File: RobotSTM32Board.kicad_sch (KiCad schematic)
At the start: 74 parts, among them IC1 TB6612FNG, IC2 TB6612FNG, J1 MotorA, J10 Qwiik1, J11 Qwiik2, J12 Qwiik3, J13 Qwiik4, J14 Qwiik5, J2 MotorB, J3 MotorC, J4 MotorD, J5 EncoderA, J6 EncoderB, J7 EncoderC, J8 EncoderD, J9 ESTOP, Q1 NPN, Q2 NMOS_Substrate, Q3 NMOS_Substrate, U1 NUCLEO-F411RE, U3 TPS564252DRLR, U4 TPS51386RJNR, U5 LM27403SQ/NOPB

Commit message: .
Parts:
- added J15: DCIn, Connector_JST:JST_XH_B2B-XH-AM_1x02_P2.50mm_Vertical, symbol Connector:Conn_01x02_Socket
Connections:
- net GND: now also U5.6 (SYNC)
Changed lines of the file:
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@@
 	)
 	(junction
+		(at 396.24 173.99)
+		(diameter 0)
+		(color 0 0 0 0)
+	)
+	(junction
 		(at 283.21 234.95)
 		(diameter 0)
@@
 	(wire
 		(pts
+			(xy 425.45 92.71) (xy 396.24 92.71)
+		)
+		(stroke
+			(width 0)
+			(type default)
+		)
+	)
+	(wire
+		(pts
 			(xy 25.4 21.59) (xy 25.4 25.4)
 		)
@@
 	(wire
 		(pts
-			(xy 381 173.99) (xy 407.67 173.99)
+			(xy 381 173.99) (xy 396.24 173.99)
 		)
 		(stroke
@@
 	(wire
 		(pts
+			(xy 396.24 92.71) (xy 396.24 173.99)
+		)
+		(stroke
+			(width 0)
+			(type default)
+		)
+	)
+	(wire
+		(pts
 			(xy 162.56 229.87) (xy 195.58 229.87)
 		)
@@
 	(wire
 		(pts
+			(xy 396.24 173.99) (xy 407.67 173.99)
+		)
+		(stroke
+			(width 0)
+			(type default)
+		)
+	)
+	(wire
+		(pts
 			(xy 303.53 242.57) (xy 303.53 243.84)
 		)
@@
 					(unit 1)
 				)
+			)
+		)
+	)
+	(symbol
+		(lib_id "Connector:Conn_01x02_Socket")
+		(at 224.79 57.15 0)
+		(unit 1)
+		(exclude_from_sim no)
+		(in_bom yes)
+		(on_board yes)
+		(dnp no)
+		(fields_autoplaced yes)
+		(property "Reference" "J15"
+			(at 226.06 57.1499 0)
+			(effects
+				(font
+					(size 1.27 1.27)
+				)
+				(justify left)
+			)
+		)
+		(property "Value" "DCIn"
+			(at 226.06 59.6899 0)
+			(effects
+				(font
+					(size 1.27 1.27)
+				)
+				(justify left)
+			)
+		)
+		(property "Footprint" "Connector_JST:JST_XH_B2B-XH-AM_1x02_P2.50mm_Vertical"
+			(at 224.79 57.15 0)
+			(effects
+				(font
+					(size 1.27 1.27)
+				)
+				(hide yes)
+			)
+		)
+		(property "Datasheet" "~"
+			(at 224.79 57.15 0)
+			(effects
+				(font
+					(size 1.27 1.27)
+				)
+				(hide yes)
+			)
+		)
+		(property "Description" "Generic connector, single row, 01x02, script generated"
+			(at 224.79 57.15 0)
+			(effects
+				(font
+					(size 1.27 1.27)
+				)
+				(hide yes)
+			)
+		)
+		(pin "2"
+		)
+		(pin "1"
+		)
+		(instances
+			(project "RobotSTM32Board"
+				(path "/ac0c4a11-3af6-428a-b627-4ab879a3dd88"
+					(reference "J15")
+					(unit 1)
+				)

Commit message: pcb routed
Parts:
- added C31, C32: 10nF, Capacitor_SMD:C_0603_1608Metric, symbol Device:C_Small
- added J16: UJC-H-G-SMT-2-P6-TR, USBCC:UJCHGSMT2P6TR, symbol UJC-H-G-SMT-2-P6-TR:UJC-H-G-SMT-2-P6-TR
- added R1, R20: 47k, Resistor_SMD:R_0603_1608Metric, symbol Device:R_Small
- added R2, R21: 20k, Resistor_SMD:R_0603_1608Metric, symbol Device:R_Small
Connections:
- net +5V: now also U1.CN7_24 (VIN)
- net ESTOP: now also U1.CN10_13 (PA6)
- net EncoderA1: now also U1.CN7_1 (PC10)
- net EncoderA2: now also U1.CN7_2 (PC11)
- net EncoderB1: now also U1.CN7_3 (PC12)
- net EncoderB2: now also U1.CN7_4 (PD2)
- net EncoderC1: now also U1.CN7_13 (PA13)
- net EncoderC2: now also U1.CN7_15 (PA14)
- net EncoderD1: now also U1.CN7_17 (PA15)
- net EncoderD2: now also U1.CN7_21 (PB7)
- net GND: now also U1.CN10_9 (GND_9), U1.CN7_19 (GND_19), U1.CN7_22 (GND_22), U1.CN7_8 (GND_8), C31.2, C32.2, R2.2, R21.2
- net MotorACCW: now also U1.CN10_15 (PA7); no longer U1.CN7_2 (PC11)
- net MotorACW: now also U1.CN10_16 (PB12); no longer U1.CN7_3 (PC12)
- net MotorBCCW: now also U1.CN10_14 (PA11); no longer U1.CN7_4 (PD2)
- net MotorBCW: now also U1.CN10_12 (PA12); no longer U1.CN7_13 (PA13)
- net MotorCCCW: now also U1.CN10_6 (PC5)
- net MotorCCW: now also U1.CN10_3 (PB8)
- net MotorDCCW: now also U1.CN10_4 (PC6)
- net MotorDCW: now also U1.CN10_1 (PC9)
- net MotorPWMA: now also U1.CN10_17 (PB6); no longer U1.CN7_1 (PC10)
- net MotorPWMB: now also U1.CN10_11 (PA5)
- net MotorPWMC: now also U1.CN10_5 (PB9)
- net MotorPWMD: now also U1.CN10_2 (PC8)
- net SCL: now also U1.CN10_23 (PA8)
- net SDA: now also U1.CN10_27 (PB4)
- net Vin: now also R1.1, R20.1; no longer U3.5 (EN)
- net at U5.7 (UVLO/EN): now also C32.1, R20.2, R21.1
- new net: C31.1, R1.2, R2.1, U3.5 (EN)
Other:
- moved on the sheet: C2, C3, C4, R10

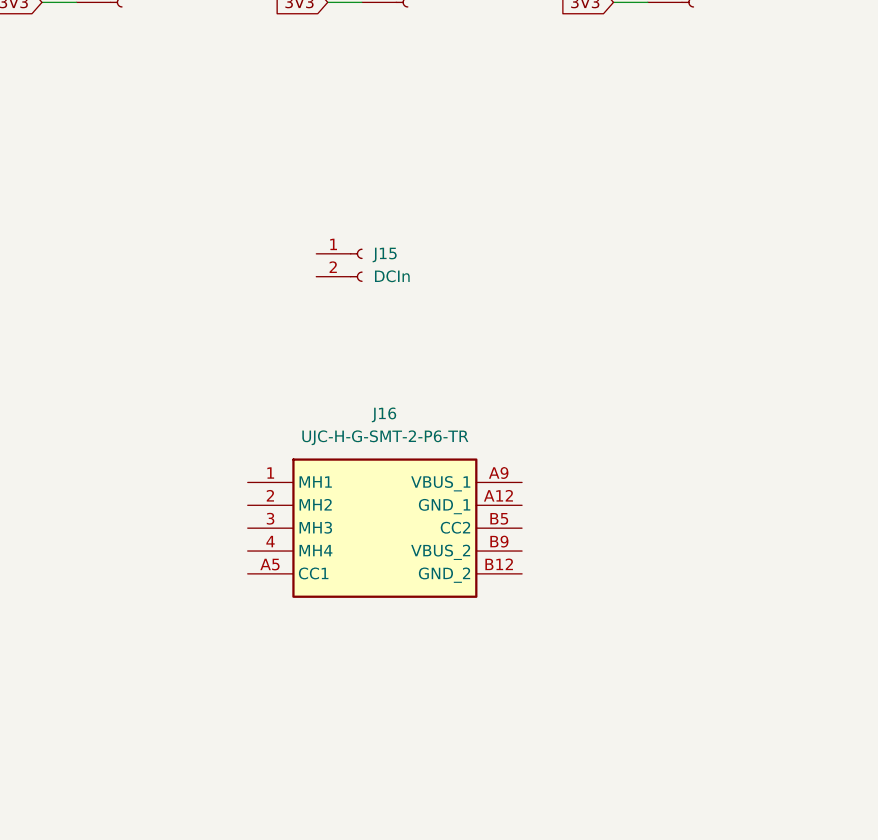
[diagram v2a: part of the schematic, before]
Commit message: correcting DRC's
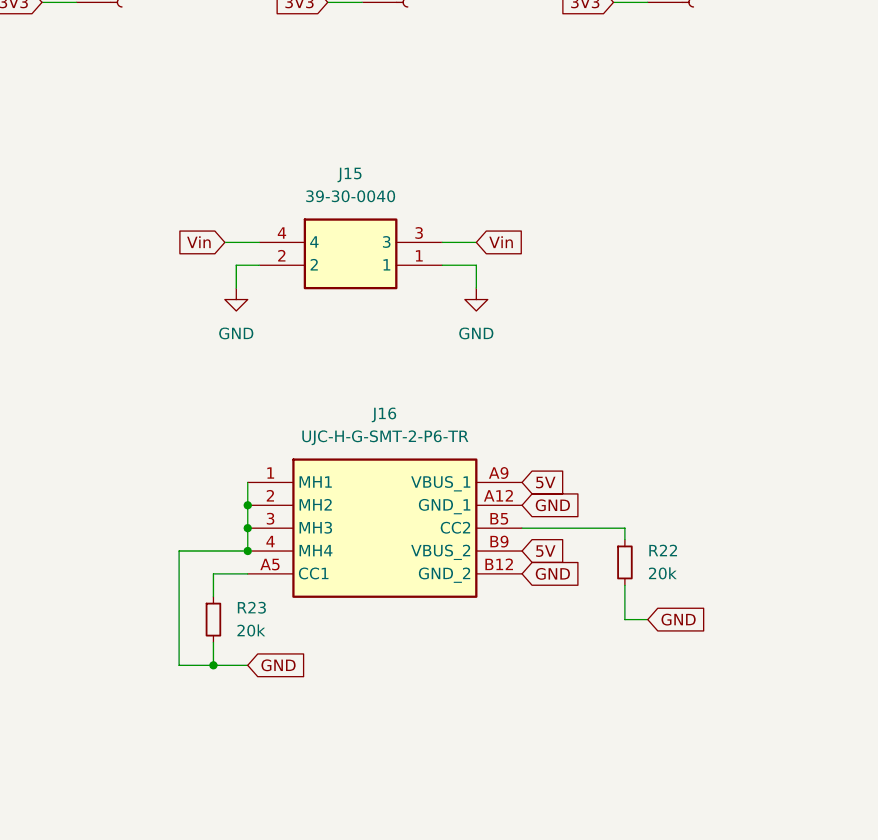
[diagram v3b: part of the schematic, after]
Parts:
- removed J15: DCIn, Connector_JST:JST_XH_B2B-XH-AM_1x02_P2.50mm_Vertical, symbol Connector:Conn_01x02_Socket
- added J15: 39-30-0040, 39-30-Y040, symbol 39-30-0040:39-30-0040
- added R22, R23: 20k, Resistor_SMD:R_0603_1608Metric, symbol Device:R_Small
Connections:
- net +5V: now also J16.A9 (VBUS_1), J16.B9 (VBUS_2)
- net GND: now also J16.1 (MH1), J16.2 (MH2), J16.3 (MH3), J16.4 (MH4), J16.A12 (GND_1), J16.B12 (GND_2), J15.1, J15.2, R22.2, R23.2
- net Vin: now also J15.3, J15.4
- net at J16.A5 (CC1): now also R23.1
- net at J16.B5 (CC2): now also R22.1

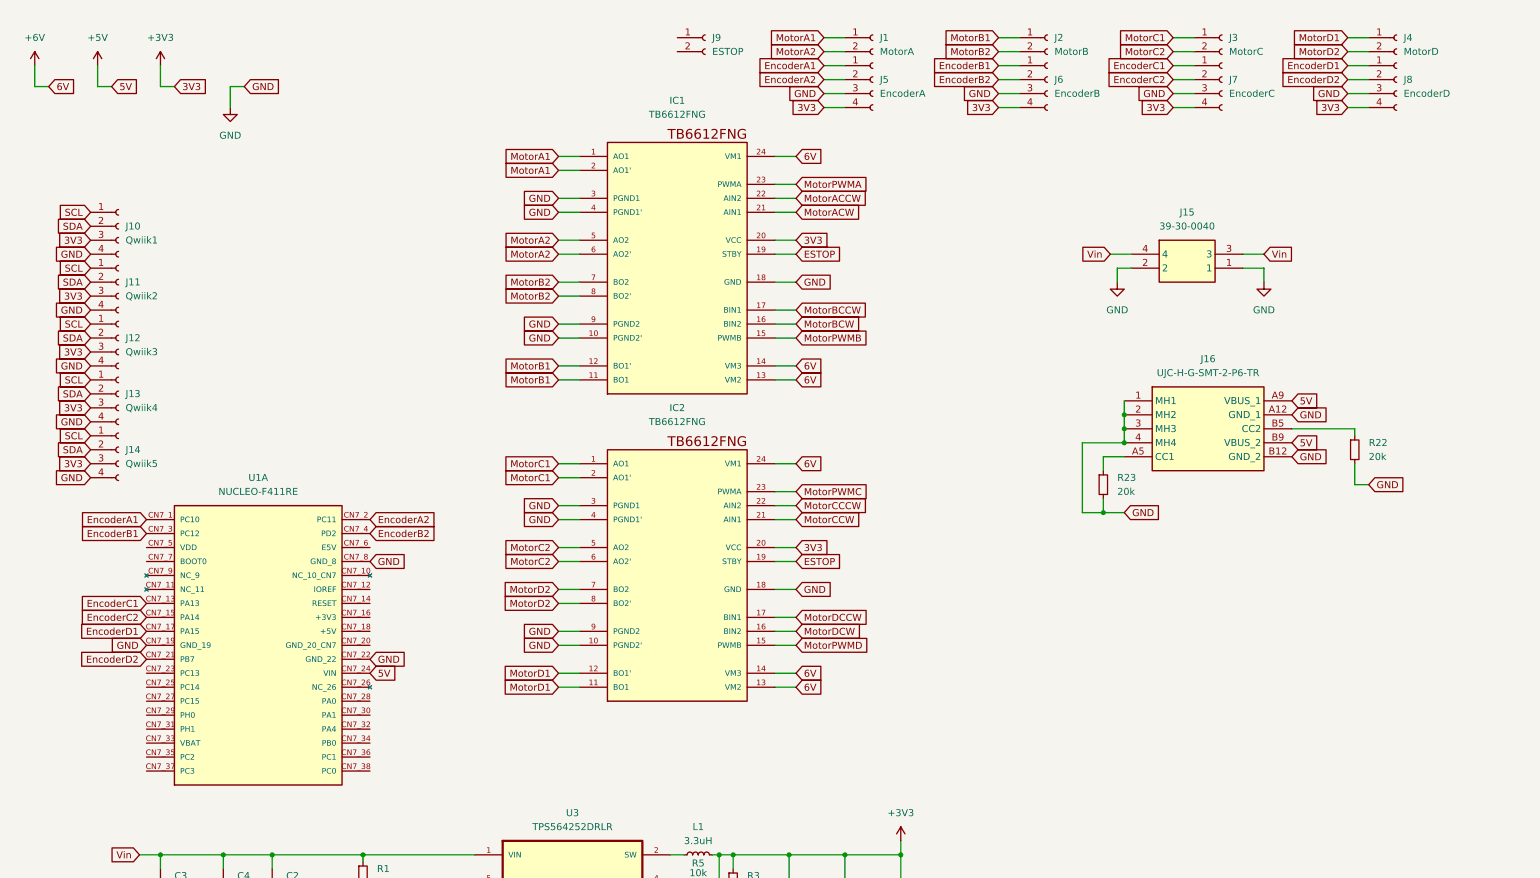
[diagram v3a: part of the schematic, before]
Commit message: Added battery connectors
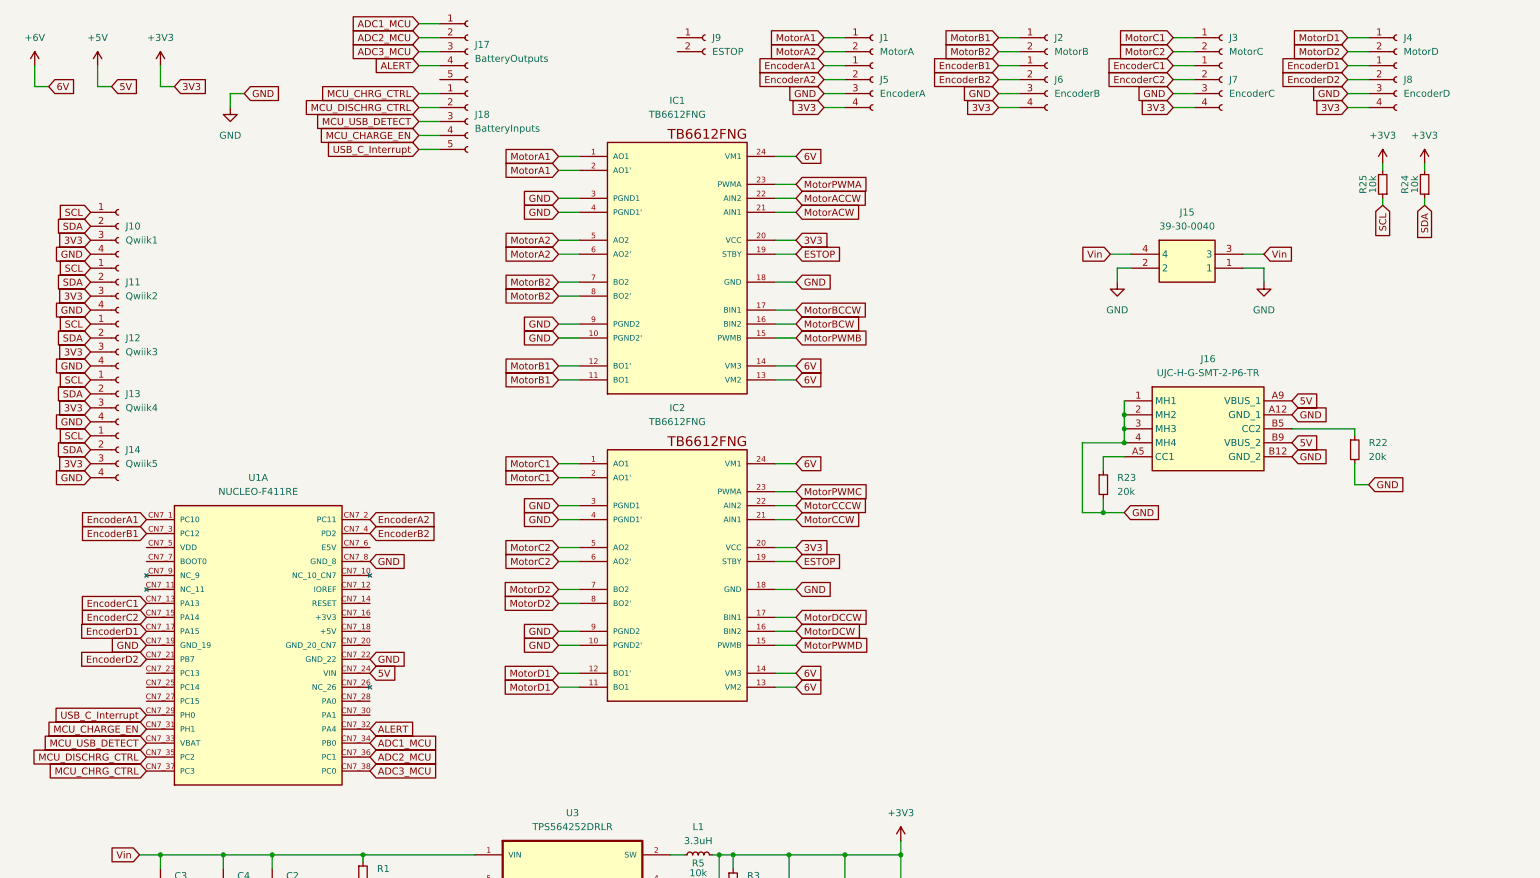
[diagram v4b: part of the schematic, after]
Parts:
- added J17: BatteryOutputs, Connector_JST:JST_SH_BM05B-SRSS-TB_1x05-1MP_P1.00mm_Vertical, symbol Connector:Conn_01x05_Socket
- added J18: BatteryInputs, Connector_JST:JST_SH_BM05B-SRSS-TB_1x05-1MP_P1.00mm_Vertical, symbol Connector:Conn_01x05_Socket
- added R24, R25: 10k, Resistor_SMD:R_0603_1608Metric, symbol Device:R_Small
- J15: footprint 39-30-Y040 -> KiCad:39-30-Y040
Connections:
- net +3V3: now also R24.2, R25.2
- net SCL: now also R25.1
- net SDA: now also R24.1
- net USB_C_Interrupt: now reaches U1.CN7_29 (PH0)
- net USB_C_Interrupt: now also J18.5 (Pin_5)
- net MCU_CHARGE_EN: now reaches U1.CN7_31 (PH1)
- net MCU_CHARGE_EN: now also J18.4 (Pin_4)
- net ALERT: now reaches U1.CN7_32 (PA4)
- net ALERT: now also J17.4 (Pin_4)
- net MCU_USB_DETECT: now reaches U1.CN7_33 (VBAT)
- net MCU_USB_DETECT: now also J18.3 (Pin_3)
- net ADC1_MCU: now reaches U1.CN7_34 (PB0)
- net ADC1_MCU: now also J17.1 (Pin_1)
- net MCU_DISCHRG_CTRL: now reaches U1.CN7_35 (PC2)
- net MCU_DISCHRG_CTRL: now also J18.2 (Pin_2)
- net ADC2_MCU: now reaches U1.CN7_36 (PC1)
- net ADC2_MCU: now also J17.2 (Pin_2)
- net MCU_CHRG_CTRL: now reaches U1.CN7_37 (PC3)
- net MCU_CHRG_CTRL: now also J18.1 (Pin_1)
- net ADC3_MCU: now reaches U1.CN7_38 (PC0)
- net ADC3_MCU: now also J17.3 (Pin_3)

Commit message: added fuse
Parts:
- added F1: 5A, symbol Device:Fuse_Small
- added TP1, TP2, TP3, TP4: TestPoint, symbol Connector:TestPoint
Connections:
- net +3V3: now also TP1.1
- net +5V: now also TP2.1
- net +6V: now also TP3.1
- net Vin: now also F1.1, TP4.1; no longer J15.3, J15.4
- new net +12V: F1.2, J15.3, J15.4

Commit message: commit of the finished thing before i tidy it up for the report
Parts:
- removed J14: Qwiik5, Connector_JST:JST_SH_BM04B-SRSS-TB_1x04-1MP_P1.00mm_Vertical, symbol Connector:Conn_01x04_Socket
- added H1, H2, H3, H4: MountingHole, MountingHole:MountingHole_2.5mm, symbol Mechanical:MountingHole
- F1: footprint (none) -> Resistor_SMD:R_0603_1608Metric
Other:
- moved on the sheet: R6
